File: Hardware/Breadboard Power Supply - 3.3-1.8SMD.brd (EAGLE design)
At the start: 54.6 x 16.5 mm, 29 parts, among them J1 POWER_JACKSMD, U1 V_REG_317SMD

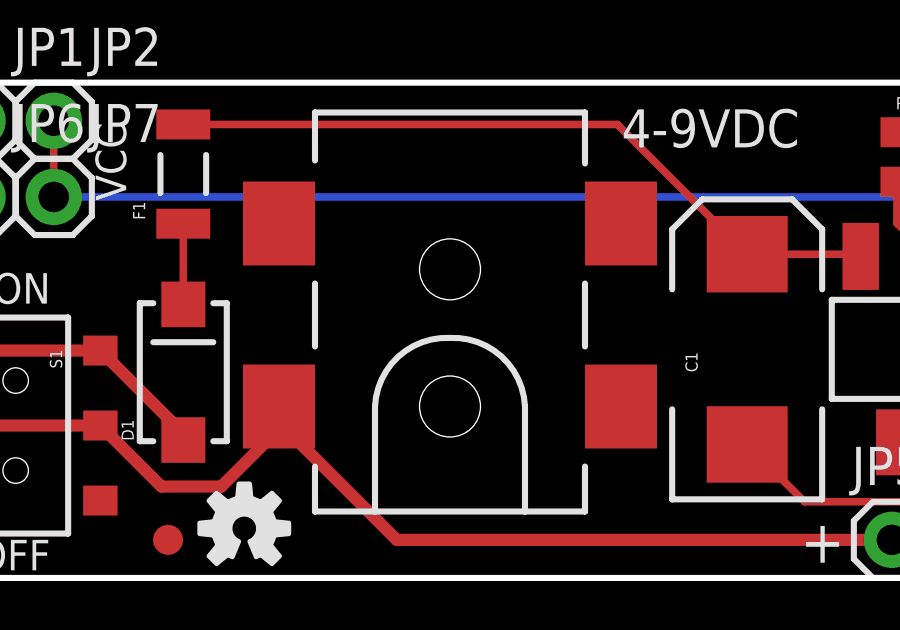
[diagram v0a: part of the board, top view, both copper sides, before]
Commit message: changed barrel jack footprint
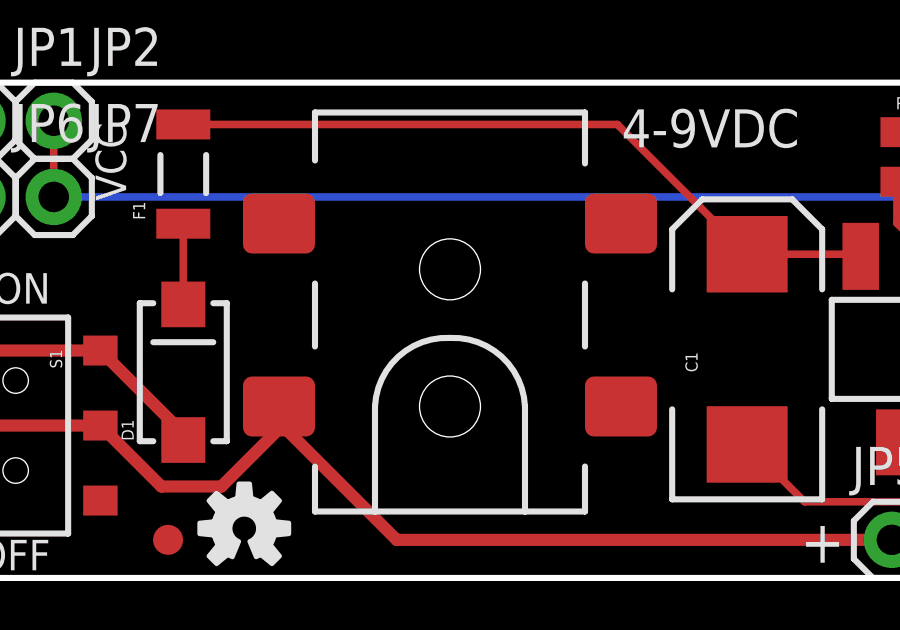
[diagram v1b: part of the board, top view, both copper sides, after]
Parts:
- J1: value POWER_JACKSMD -> POWER_JACKOVERPASTE_REDBOARD_0603; device SparkFun-Connectors:POWER_JACK_SMD -> Testing:POWER_JACK_SMD_OVERPASTE_REDBOARD_0603

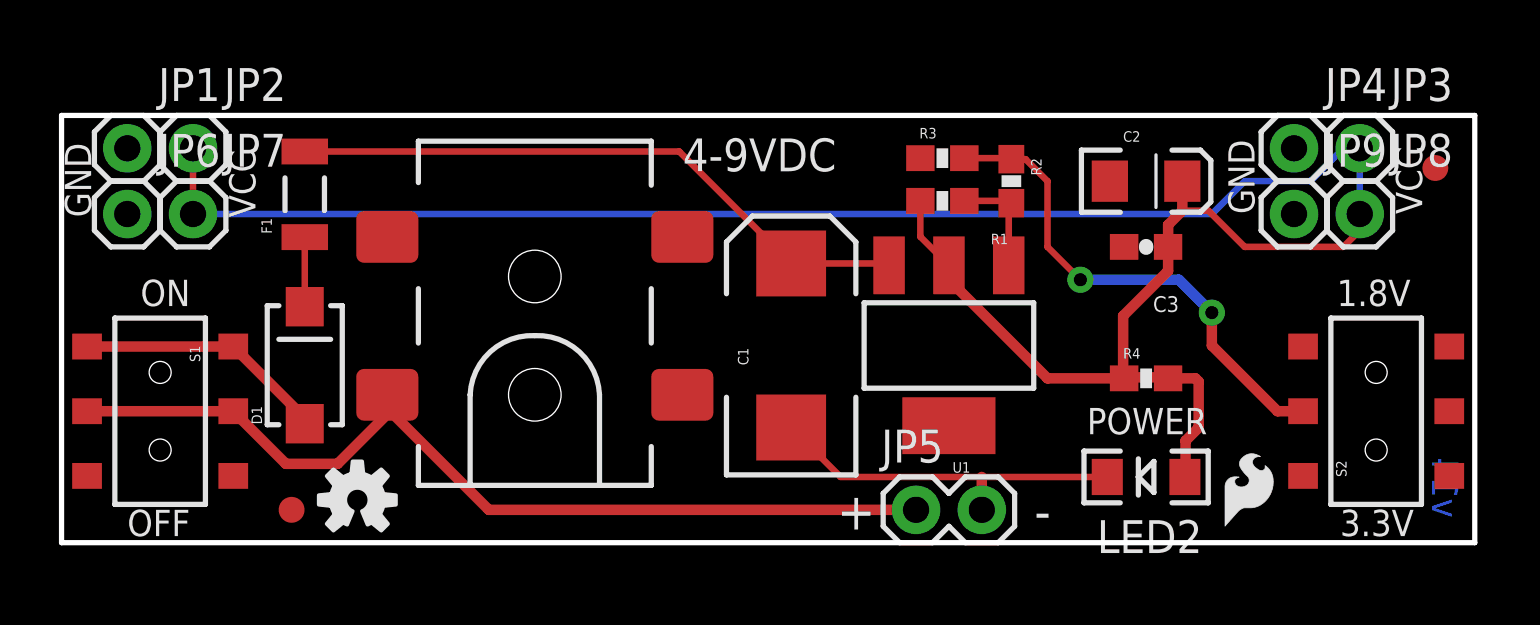
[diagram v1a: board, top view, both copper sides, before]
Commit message: Changed RES position, fixed airwires
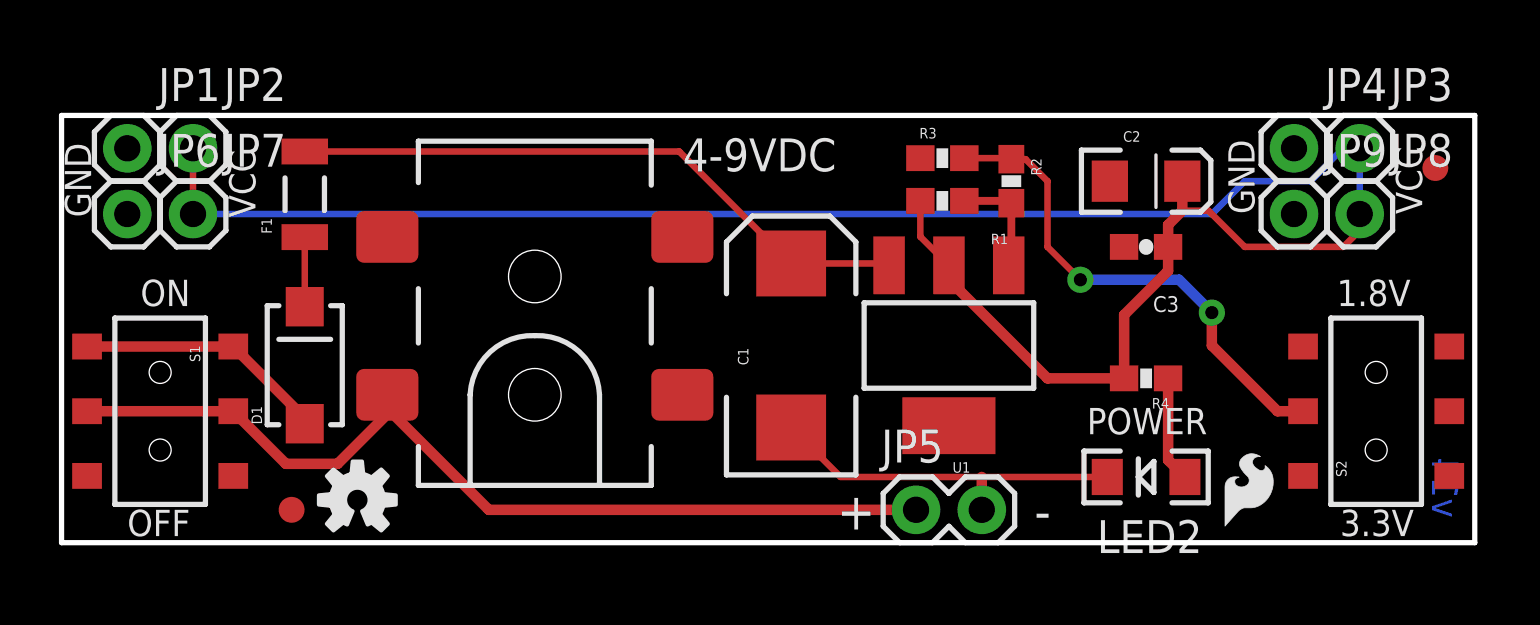
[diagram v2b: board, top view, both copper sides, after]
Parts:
- turned R4 to 180 degrees
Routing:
- net VCC: track 82.2 -> 80.4 mm
- net N$8: track 4.72 -> 4.08 mm
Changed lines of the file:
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@@
 </class>
 </classes>
-<designrules name="SparkFun *">
+<designrules name="SparkFun-2-layer">
 <description language="en">&lt;b&gt;EAGLE Design Rules&lt;/b&gt;
 &lt;p&gt;
@@
 <param name="mdViaViaSameLayer" value="8mil"/>
 <param name="mnLayersViaInSmd" value="2"/>
-<param name="mdCopperDimension" value="10mil"/>
+<param name="mdCopperDimension" value="8mil"/>
 <param name="mdDrill" value="8mil"/>
 <param name="mdSmdStop" value="0mil"/>
-<param name="msWidth" value="8mil"/>
-<param name="msDrill" value="20mil"/>
+<param name="msWidth" value="7mil"/>
+<param name="msDrill" value="15mil"/>
 <param name="msMicroVia" value="9.99mm"/>
 <param name="msBlindViaRatio" value="0.5"/>
@@
 <element name="JP8" library="SparkFun" package="1X01" value="M01PTH" x="50.165" y="12.7"/>
 <element name="JP9" library="SparkFun" package="1X01" value="M01PTH" x="47.625" y="12.7"/>
-<element name="R4" library="SparkFun-Resistors" package="0603-RES" value="240" x="41.91" y="6.35">
-<attribute name="PROD_ID" value="RES-07849" x="41.91" y="6.35" size="1.778" layer="27" font="vector" ratio="15" display="off"/>
+<element name="R4" library="SparkFun-Resistors" package="0603-RES" value="240" x="41.91" y="6.35" rot="R180">
+<attribute name="PROD_ID" value="RES-07849" x="41.91" y="6.35" size="1.778" layer="27" font="vector" ratio="15" rot="R180" display="off"/>
 </element>
 <element name="R2" library="SparkFun-Resistors" package="0603-RES" value="105" x="36.703" y="13.97" rot="R270">
@@
 <contactref element="R1" pad="1"/>
 <contactref element="U1" pad="1"/>
-<wire x1="36.6014" y1="10.7188" x2="36.6014" y2="13.1454" width="0.254" layer="1"/>
-<wire x1="34.886" y1="13.208" x2="36.664" y2="13.208" width="0.254" layer="1"/>
 <contactref element="R2" pad="2"/>
-<wire x1="36.664" y1="13.208" x2="36.703" y2="13.12" width="0" layer="19" extent="1-1"/>
-<wire x1="36.6014" y1="13.1454" x2="36.664" y2="13.208" width="0" layer="19" extent="1-1"/>
+<wire x1="36.6014" y1="10.7188" x2="36.703" y2="10.7188" width="0.3048" layer="1"/>
+<wire x1="36.703" y1="10.7188" x2="36.703" y2="13.12" width="0.3048" layer="1"/>
+<wire x1="34.886" y1="13.208" x2="36.615" y2="13.208" width="0.3048" layer="1"/>
+<wire x1="36.615" y1="13.208" x2="36.703" y2="13.12" width="0.3048" layer="1"/>
 </signal>
 <signal name="N$8">
 <contactref element="LED2" pad="A"/>
-<wire x1="43.815" y1="6.35" x2="43.942" y2="6.223" width="0.4064" layer="1"/>
-<wire x1="43.942" y1="6.223" x2="43.942" y2="4.445" width="0.4064" layer="1"/>
-<wire x1="43.942" y1="4.445" x2="43.434" y2="3.937" width="0.4064" layer="1"/>
-<wire x1="43.434" y1="3.937" x2="43.434" y2="2.564" width="0.4064" layer="1"/>
-<wire x1="43.434" y1="2.564" x2="43.41" y2="2.54" width="0.4064" layer="1"/>
 <contactref element="R4" pad="1"/>
-<wire x1="43.815" y1="6.35" x2="43.18" y2="6.35" width="0.4064" layer="1"/>
-<wire x1="41.06" y1="6.35" x2="43.18" y2="6.35" width="0" layer="19" extent="1-1"/>
+<wire x1="43.41" y1="2.54" x2="42.76" y2="3.19" width="0.4064" layer="1"/>
+<wire x1="42.76" y1="3.19" x2="42.76" y2="6.35" width="0.4064" layer="1"/>
 </signal>
 <signal name="RAW">
@@
 <wire x1="48.26" y1="13.97" x2="45.72" y2="13.97" width="0.254" layer="16"/>
 <wire x1="45.72" y1="13.97" x2="44.45" y2="12.7" width="0.254" layer="16"/>
-<wire x1="44.45" y1="12.7" x2="5.08" y2="12.7" width="0.254" layer="16"/>
+<wire x1="5.08" y1="12.7" x2="44.45" y2="12.7" width="0.254" layer="16"/>
 <wire x1="50.165" y1="15.24" x2="49.53" y2="15.24" width="0.254" layer="16"/>
 <wire x1="33.186" y1="13.208" x2="33.186" y2="11.8228" width="0.254" layer="1"/>
@@
 <wire x1="34.29" y1="10.16" x2="38.1" y2="6.35" width="0.4064" layer="1"/>
 <wire x1="42.76" y1="11.43" x2="42.76" y2="10.502" width="0.4064" layer="1"/>
-<wire x1="42.76" y1="10.502" x2="41.021" y2="8.763" width="0.4064" layer="1"/>
-<wire x1="41.021" y1="8.763" x2="41.021" y2="6.389" width="0.4064" layer="1"/>
 <contactref element="R4" pad="2"/>
-<wire x1="38.1" y1="6.35" x2="40.982" y2="6.35" width="0.4064" layer="1"/>
-<wire x1="40.982" y1="6.35" x2="41.021" y2="6.389" width="0.4064" layer="1"/>
-<wire x1="41.021" y1="6.389" x2="42.721" y2="6.389" width="0.4064" layer="1"/>
-<wire x1="42.721" y1="6.389" x2="42.76" y2="6.35" width="0.4064" layer="1"/>
+<wire x1="38.1" y1="6.35" x2="41.06" y2="6.35" width="0.4064" layer="1"/>
+<wire x1="42.76" y1="10.502" x2="41.06" y2="8.802" width="0.4064" layer="1"/>
+<wire x1="41.06" y1="8.802" x2="41.06" y2="6.35" width="0.4064" layer="1"/>
 </signal>
 <signal name="N$1">
